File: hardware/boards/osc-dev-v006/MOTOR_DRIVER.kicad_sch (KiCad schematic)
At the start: 18 parts, among them J3 PIN-1-3P, U2 DRV8212PDSGR

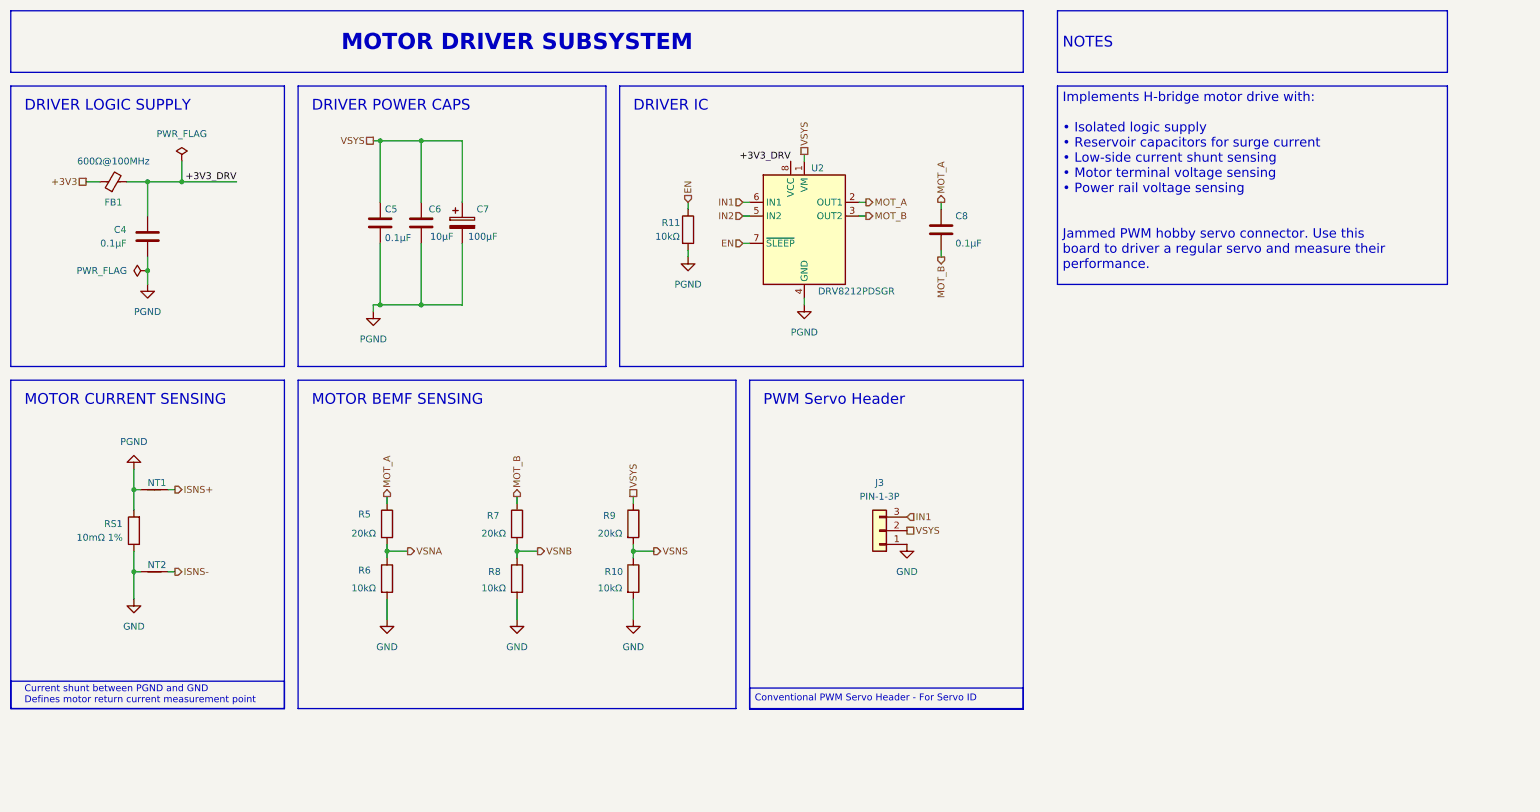
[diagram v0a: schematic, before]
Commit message: hw: osc-dev-v006 rev-2a - 6l precision respin, direct-wire bus, docs
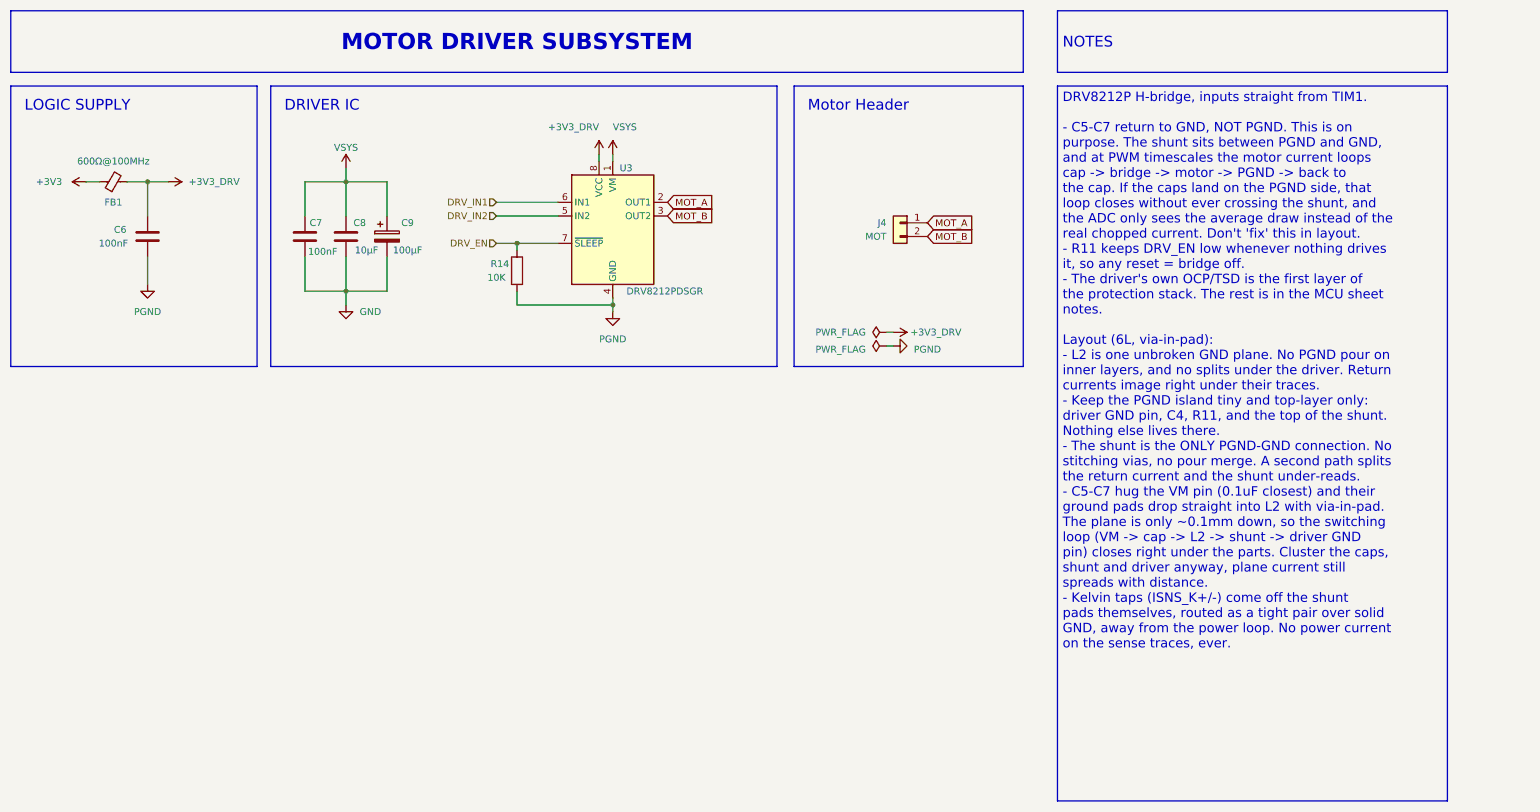
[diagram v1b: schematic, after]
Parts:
- removed C8: 0.1µF, Capacitor_SMD:C_0805_2012Metric_Pad1.18x1.45mm_HandSolder, symbol Device:C
- removed J3: PIN-1-3P, Connector_PinHeader_2.54mm:PinHeader_1x03_P2.54mm_Vertical, symbol Connector_Generic:Conn_01x03
- removed NT1, NT2: NetTie_2, shared:NetTie-2_SMD_0.2mm, symbol Device:NetTie_2
- removed R10, R11, R6, R8: 10kΩ, Resistor_SMD:R_0805_2012Metric_Pad1.20x1.40mm_HandSolder, symbol Device:R
- removed R5, R7, R9: 20kΩ, Resistor_SMD:R_0805_2012Metric_Pad1.20x1.40mm_HandSolder, symbol Device:R
- removed RS1: 10mΩ 1%, Resistor_SMD:R_1206_3216Metric, symbol Device:R
- added J4: MOT, Connector_PinHeader_2.54mm:PinHeader_1x02_P2.54mm_Vertical, symbol Connector_Generic:Conn_01x02
- added R14: 10K, Resistor_SMD:R_0603_1608Metric_Pad0.98x0.95mm_HandSolder, symbol Device:R
- C6: renamed from C4; value 0.1µF -> 100nF; footprint Capacitor_SMD:C_0805_2012Metric_Pad1.18x1.45mm_HandSolder -> Capacitor_SMD:C_0603_1608Metric_Pad1.08x0.95mm_HandSolder; LCSC C28233 -> C24452
- C7: renamed from C5; value 0.1µF -> 100nF; footprint Capacitor_SMD:C_0805_2012Metric_Pad1.18x1.45mm_HandSolder -> Capacitor_SMD:C_0603_1608Metric_Pad1.08x0.95mm_HandSolder; LCSC C28233 -> C24452
- C8: renamed from C6; LCSC C440198 -> C15850; MFPN GRM21BR61H106KE43L -> CL21A106KAYNNNE
- FB1: footprint Inductor_SMD:L_0805_2012Metric_Pad1.05x1.20mm_HandSolder -> Inductor_SMD:L_0603_1608Metric_Pad1.05x0.95mm_HandSolder; LCSC C1017 -> C108301
- U3: renamed from U2; footprint Package_SON:WSON-8-1EP_2x2mm_P0.5mm_EP0.9x1.6mm -> Package_SON:Texas_DSG0008A_WSON-8-1EP_2x2mm_P0.5mm_EP0.9x1.6mm
- renumbered C7 to C9
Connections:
- net GND: now also C7.2, C8.2, C9.2
- net MOT_A: now also J4.1 (Pin_1)
- net MOT_B: now also J4.2 (Pin_2)
- net PGND: now also R14.2; no longer C7.2, C8.2, C9.2
- net EN renamed DRV_EN
- net DRV_EN: now also R14.1
- net IN1 renamed DRV_IN1
- net IN2 renamed DRV_IN2
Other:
- note added: "LOGIC SUPPLY"
- note added: "Motor Header"
- note removed: "Current shunt between PGND and GND Defines motor return current measurement point"
- note removed: "DRIVER LOGIC SUPPLY"
- note removed: "DRIVER POWER CAPS"
- note removed: "MOTOR BEMF SENSING"
- note removed: "MOTOR CURRENT SENSING"
- note removed: "PWM Servo Header"
- title: (none) -> ${PROJECT} / ${BOARD}
- moved on the sheet: C7, C8, C9, U3

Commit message: hw: v006 lcsc fields track rev-2a order substitutions
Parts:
- C6, C7: LCSC C24452 -> C14663; MFPN CL21B104KCFNNNE -> CC0603KRX7R9BB104
- C9: LCSC C19271225 -> C22383777; MFPN VT1V101M-CRE54 -> VT1V101M0605
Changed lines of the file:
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@@
 			)
 		)
-		(property "Datasheet" "https://www.lcsc.com/product-detail/C19271225.html"
+		(property "Datasheet" "https://www.lcsc.com/product-detail/C22383777.html"
 			(at 85.09 55.88 0)
 			(hide yes)
@@
 			)
 		)
-		(property "Description" "Polarized capacitor"
+		(property "Description" "100µF ±20% 35V aluminum electrolytic 6.3x5.4"
 			(at 85.09 55.88 0)
 			(hide yes)
@@
 			)
 		)
-		(property "LCSC" "C19271225"
+		(property "LCSC" "C22383777"
 			(at 82.55 53.34 0)
 			(hide yes)
@@
 			)
 		)
-		(property "MFPN" "VT1V101M-CRE54"
+		(property "MFPN" "VT1V101M0605"
 			(at 82.55 53.34 0)
 			(hide yes)
@@
 			)
 		)
-		(property "Datasheet" "https://www.lcsc.com/product-detail/C24452.html"
+		(property "Datasheet" "https://www.lcsc.com/product-detail/C14663.html"
 			(at 31.21 31.76 0)
 			(hide yes)
@@
 			)
 		)
-		(property "Description" "Unpolarized capacitor"
+		(property "Description" "100nF ±10% 50V X7R 0603"
 			(at 31.21 31.76 0)
 			(hide yes)
@@
 			)
 		)
-		(property "LCSC" "C24452"
+		(property "LCSC" "C14663"
 			(at 71.882 53.34 0)
 			(hide yes)
@@
 			)
 		)
-		(property "MFPN" "CL21B104KCFNNNE"
+		(property "MFPN" "CC0603KRX7R9BB104"
 			(at 71.882 53.34 0)
 			(hide yes)
@@
 			)
 		)
-		(property "Datasheet" "https://www.lcsc.com/product-detail/C24452.html"
+		(property "Datasheet" "https://www.lcsc.com/product-detail/C14663.html"
 			(at 14.7 21.76 0)
 			(hide yes)
@@
 			)
 		)
-		(property "Description" "Unpolarized capacitor"
+		(property "Description" "100nF ±10% 50V X7R 0603"
 			(at 14.7 21.76 0)
 			(hide yes)
@@
 			)
 		)
-		(property "LCSC" "C24452"
+		(property "LCSC" "C14663"
 			(at 38.1 53.34 0)
 			(hide yes)
@@
 			)
 		)
-		(property "MFPN" "CL21B104KCFNNNE"
+		(property "MFPN" "CC0603KRX7R9BB104"
 			(at 38.1 53.34 0)
 			(hide yes)

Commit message: board: v006 rev-2a schematic refresh, family designators, terminal bias, tier-2 position input
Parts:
- removed C6: 100nF, Capacitor_SMD:C_0603_1608Metric_Pad1.08x0.95mm_HandSolder, symbol Device:C
- removed FB1: 600Ω@100MHz, Inductor_SMD:L_0603_1608Metric_Pad1.05x0.95mm_HandSolder, symbol Device:FerriteBead_Small
- added Ch1: 100nF, Capacitor_SMD:C_0603_1608Metric_Pad1.08x0.95mm_HandSolder, symbol Device:C
- added Ch4: 10uF, Capacitor_SMD:C_0805_2012Metric_Pad1.18x1.45mm_HandSolder, symbol Device:C
- Ch3: renamed from C8; value 10µF -> 10uF
- Ch5: renamed from C9; value 100µF -> 100uF
- J4: LCSC (none) -> C492401; MFPN (none) -> 2.54-1*2P
- Rh1: renamed from R14; MFPN FRC0805F1002TS -> FRC0603F1002TS
- U3: footprint Package_SON:Texas_DSG0008A_WSON-8-1EP_2x2mm_P0.5mm_EP0.9x1.6mm -> Package_SON:Texas_DSG0008A_WSON-8-1EP_2x2mm_P0.5mm_EP0.9x1.6mm_ThermalVias; JLC Type Extended -> (none)
- renumbered C7 to Ch2
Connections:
- net +3V3_DRV is gone; now on net +3V3: U3.8 (VCC)
- net +3V3: now also Ch1.1
- net GND: now also Ch1.2, Ch4.2
- net VSYS: now also Ch4.1
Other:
- note added: "Decoupling and bulk"
- note added: "Motor driver"
- note added: "Motor header"
- note removed: "DRIVER IC"
- note removed: "LOGIC SUPPLY"
- note removed: "Motor Header"
- moved on the sheet: Ch2, Ch3, Ch5

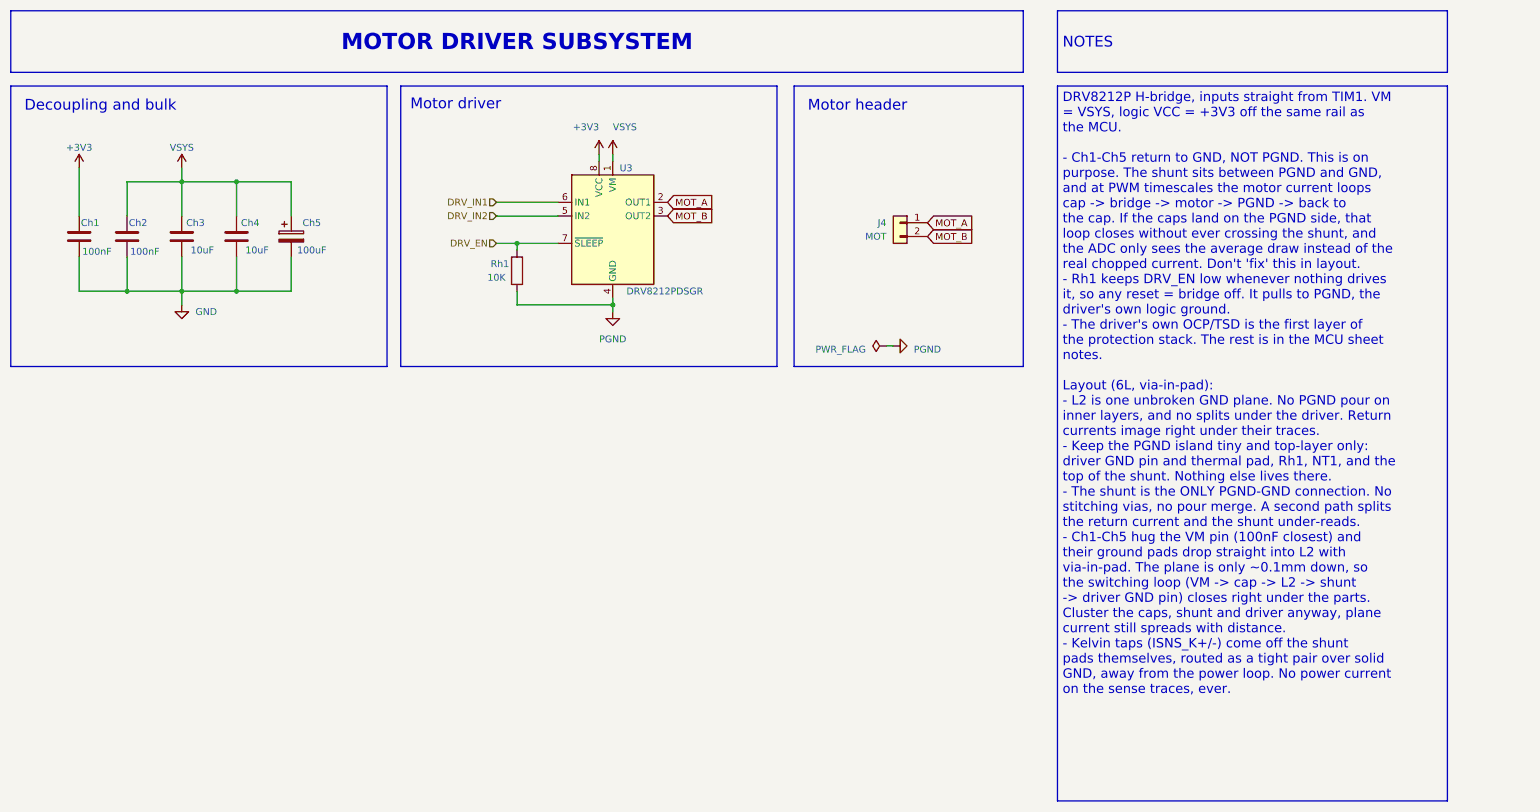
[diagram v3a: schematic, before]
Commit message: board: v006 rev-2a audit fixes, rs2 deleted, rh2 jumper on the driver rail
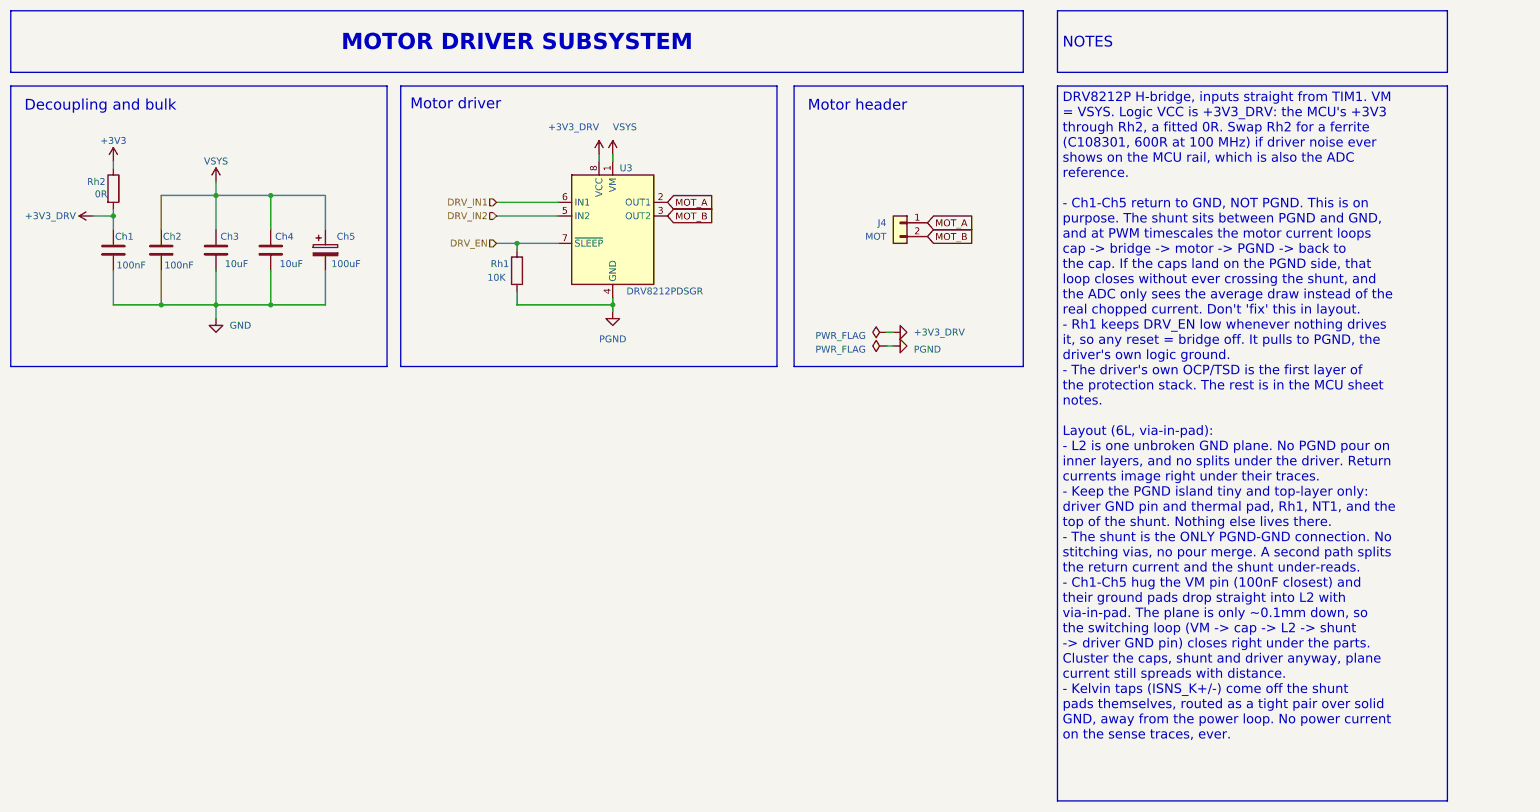
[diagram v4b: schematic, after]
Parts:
- added Rh2: 0R, Resistor_SMD:R_0603_1608Metric_Pad0.98x0.95mm_HandSolder, symbol Device:R
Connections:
- net +3V3: now also Rh2.1; no longer Ch1.1, U3.8 (VCC)
- new net +3V3_DRV: Ch1.1, Rh2.2, U3.8 (VCC)
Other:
- moved on the sheet: Ch1, Ch2, Ch3, Ch4, Ch5

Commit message: board: v006 rev-2a placement, silk labels, test point rows, silk rules
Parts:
- added TP3: IN1, TestPoint:TestPoint_Pad_D1.0mm, symbol Connector:TestPoint_Small
- added TP4: IN2, TestPoint:TestPoint_Pad_D1.0mm, symbol Connector:TestPoint_Small
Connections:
- net DRV_IN1: now also TP3.1
- net DRV_IN2: now also TP4.1
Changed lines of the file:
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@@
+	)
+	(junction
+		(at 111.76 49.53)
+		(diameter 0)
+		(color 0 0 0 0)
 	)
 	(junction
@@
 		(color 0 0 0 0)
 	)
+	(junction
+		(at 111.76 52.07)
+		(diameter 0)
+		(color 0 0 0 0)
+	)
 	(wire
 		(pts
@@
 	(wire
 		(pts
+			(xy 111.76 52.07) (xy 111.76 53.34)
+		)
+		(stroke
+			(width 0)
+			(type default)
+		)
+	)
+	(wire
+		(pts
 			(xy 73.66 54.61) (xy 73.66 48.26)
 		)
@@
 		(pts
 			(xy 127 68.58) (xy 127 67.31)
+		)
+		(stroke
+			(width 0)
+			(type default)
+		)
+	)
+	(wire
+		(pts
+			(xy 111.76 49.53) (xy 111.76 48.26)
 		)
 		(stroke
@@
 	)
 	(symbol
+		(lib_id "Connector:TestPoint_Small")
+		(at 111.76 48.26 0)
+		(unit 1)
+		(body_style 1)
+		(exclude_from_sim no)
+		(in_bom no)
+		(on_board yes)
+		(in_pos_files yes)
+		(dnp no)
+		(property "Reference" "TP3"
+			(at 111.76 46.99 0)
+			(show_name no)
+			(do_not_autoplace no)
+			(effects
+				(font
+					(size 1.27 1.27)
+				)
+			)
+		)
+		(property "Value" "IN1"
+			(at 110.49 49.53 0)
+			(hide yes)
+			(show_name no)
+			(do_not_autoplace no)
+			(effects
+				(font
+					(size 1.27 1.27)
+				)
+				(justify right)
+			)
+		)
+		(property "Footprint" "TestPoint:TestPoint_Pad_D1.0mm"
+			(at 116.84 48.26 0)
+			(hide yes)
+			(show_name no)
+			(do_not_autoplace no)
+			(effects
+				(font
+					(size 1.27 1.27)
+				)
+			)
+		)
+		(property "Datasheet" ""
+			(at 116.84 48.26 0)
+			(hide yes)
+			(show_name no)
+			(do_not_autoplace no)
+			(effects
+				(font
+					(size 1.27 1.27)
+				)
+			)
+		)
+		(property "Description" "test point"
+			(at 111.76 48.26 0)
+			(hide yes)
+			(show_name no)
+			(do_not_autoplace no)
+			(effects
+				(font
+					(size 1.27 1.27)
+				)
+			)
+		)
+		(pin "1"
+		)
+		(instances
+			(project "osc-dev-v006"
+				(path "/6062e7d2-0c72-467e-b49c-6387ba053e09/ada02f24-9f0e-4313-921a-475b46fb1a47"
+					(reference "TP3")
+					(unit 1)
+				)
+			)
+		)
+	)
+	(symbol
 		(lib_id "power:VBUS")
 		(at 34.29 41.91 0)
@@
 					(unit 1)
 				)
+			)
+		)
+	)
+	(symbol
+		(lib_id "Connector:TestPoint_Small")
+		(at 111.76 53.34 180)
+		(unit 1)
+		(body_style 1)
+		(exclude_from_sim no)
+		(in_bom no)
+		(on_board yes)
+		(in_pos_files yes)
+		(dnp no)
+		(property "Reference" "TP4"
+			(at 111.76 54.864 0)
+			(show_name no)
+			(do_not_autoplace no)
+			(effects
+				(font
+					(size 1.27 1.27)
+				)
+			)
+		)
+		(property "Value" "IN2"
+			(at 113.03 54.61 0)
+			(hide yes)
+			(show_name no)
+			(do_not_autoplace no)
+			(effects
+				(font
+					(size 1.27 1.27)
+				)
+				(justify left)
+			)
+		)
+		(property "Footprint" "TestPoint:TestPoint_Pad_D1.0mm"
+			(at 116.84 53.34 0)
+			(hide yes)
+			(show_name no)
+			(do_not_autoplace no)
+			(effects
+				(font
+					(size 1.27 1.27)
+				)
+			)
+		)
+		(property "Datasheet" ""
+			(at 116.84 53.34 0)
+			(hide yes)
+			(show_name no)
+			(do_not_autoplace no)
+			(effects
+				(font
+					(size 1.27 1.27)
+				)
+			)
+		)
+		(property "Description" "test point"
+			(at 111.76 53.34 0)
+			(hide yes)
+			(show_name no)
+			(do_not_autoplace no)
+			(effects
+				(font
+					(size 1.27 1.27)
+				)
+			)
+		)
+		(pin "1"
+		)
+		(instances
+			(project "osc-dev-v006"
+				(path "/6062e7d2-0c72-467e-b49c-6387ba053e09/ada02f24-9f0e-4313-921a-475b46fb1a47"
+					(reference "TP4")
+					(unit 1)
+				)

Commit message: board: osc-dev-v006 rev 2a board images, u3 footprint without thermal vias (#108)
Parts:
- U3: footprint Package_SON:Texas_DSG0008A_WSON-8-1EP_2x2mm_P0.5mm_EP0.9x1.6mm_ThermalVias -> Package_SON:Texas_DSG0008A_WSON-8-1EP_2x2mm_P0.5mm_EP0.9x1.6mm
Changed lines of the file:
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@@
 			)
 		)
-		(property "Footprint" "Package_SON:Texas_DSG0008A_WSON-8-1EP_2x2mm_P0.5mm_EP0.9x1.6mm_ThermalVias"
+		(property "Footprint" "Package_SON:Texas_DSG0008A_WSON-8-1EP_2x2mm_P0.5mm_EP0.9x1.6mm"
 			(at 127 76.2 0)
 			(hide yes)
